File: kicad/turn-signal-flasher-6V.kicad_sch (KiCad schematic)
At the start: 21 parts, among them J1 Conn_Blade, J2 Conn_Blade, J3 Conn_Blade, Q1 BC327, Q2 YJD70P03A, U1 ATtiny45-20P, U2 LM337_TO92

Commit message: add init FW
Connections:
- net at R8.1, R9.2: now also U1.3 (XTAL2/PB4); no longer U1.7 (PB2)
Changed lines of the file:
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@@
+	(wire
+		(pts
+			(xy 115.57 64.77) (xy 115.57 100.33)
+		)
+		(stroke
+			(width 0)
+			(type default)
+		)
+	)
+	(wire
+		(pts
+			(xy 139.7 67.31) (xy 139.7 100.33)
+		)
+		(stroke
+			(width 0)
+			(type default)
+		)
+	)
 	(wire
 		(pts
@@
 	(wire
 		(pts
-			(xy 139.7 62.23) (xy 106.68 62.23)
-		)
-		(stroke
-			(width 0)
-			(type default)
-		)
-	)
-	(wire
-		(pts
 			(xy 195.58 68.58) (xy 214.63 68.58)
 		)
@@
 	(wire
 		(pts
-			(xy 115.57 64.77) (xy 106.68 64.77)
+			(xy 106.68 67.31) (xy 139.7 67.31)
 		)
 		(stroke
@@
 	(wire
 		(pts
-			(xy 115.57 100.33) (xy 115.57 64.77)
-		)
-		(stroke
-			(width 0)
-			(type default)
-		)
-	)
-	(wire
-		(pts
 			(xy 195.58 34.29) (xy 195.58 36.83)
 		)
@@
 	(wire
 		(pts
+			(xy 106.68 64.77) (xy 115.57 64.77)
+		)
+		(stroke
+			(width 0)
+			(type default)
+		)
+	)
+	(wire
+		(pts
 			(xy 173.99 110.49) (xy 173.99 113.03)
 		)
@@
 		)
 		(stroke
-			(width 0)
-			(type default)
-		)
-	)
-	(wire
-		(pts
-			(xy 139.7 62.23) (xy 139.7 100.33)
-		)
-		(stroke

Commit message: finalize PCB and code
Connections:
- no-connect marks 0 -> 3
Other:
- title: (none) -> Turn signal flasher 6 V

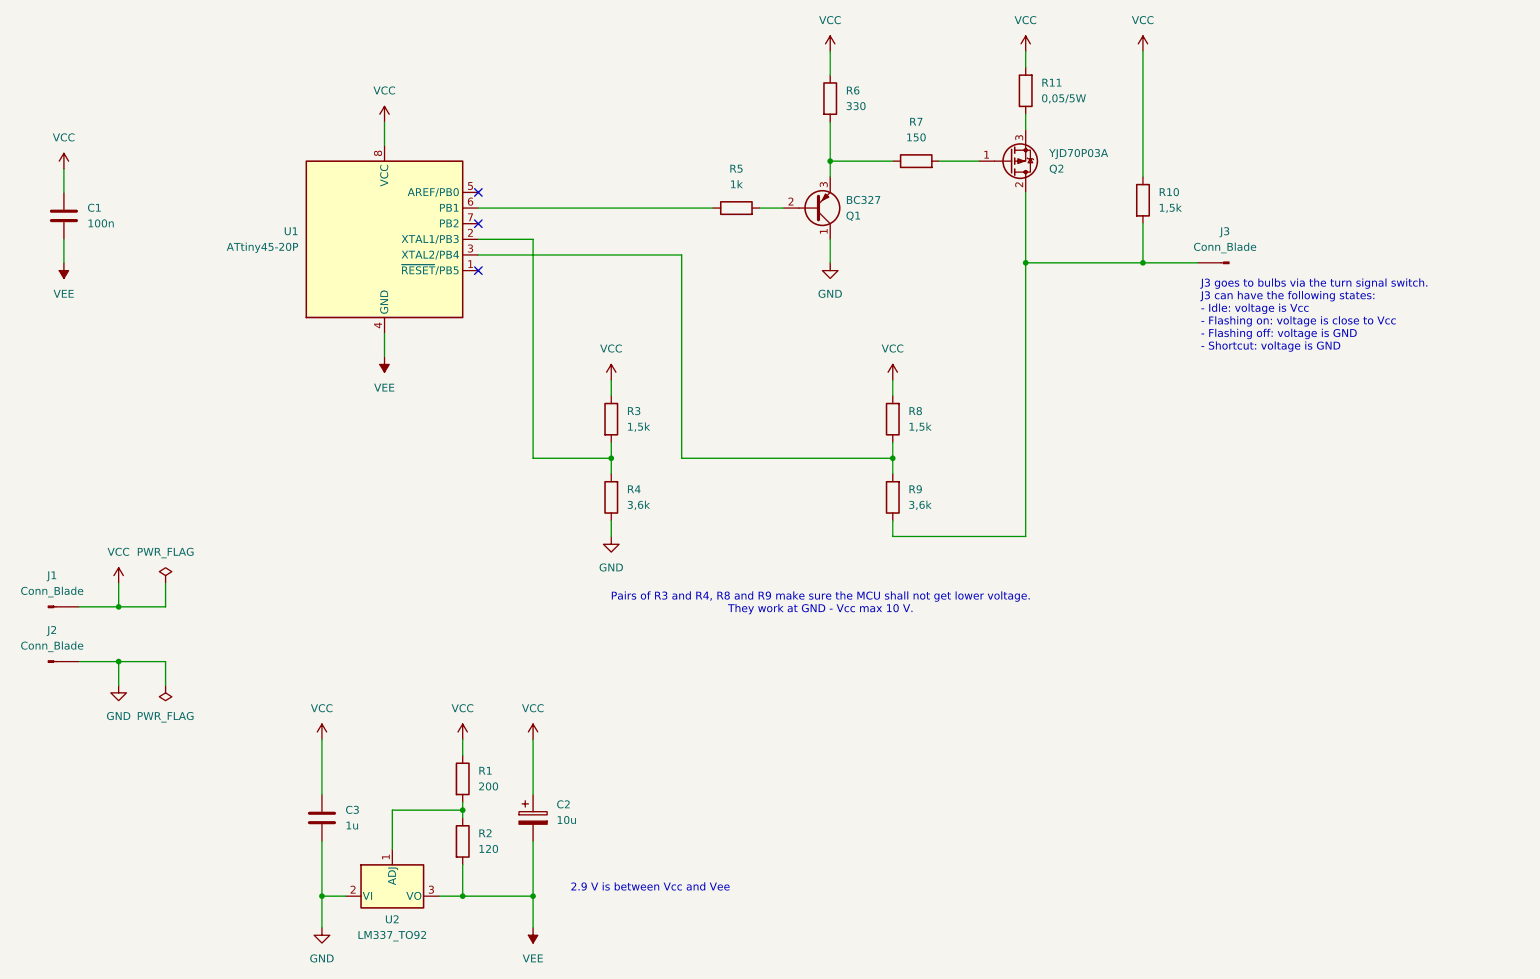
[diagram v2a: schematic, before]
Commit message: fix: overshoot of MOSFET
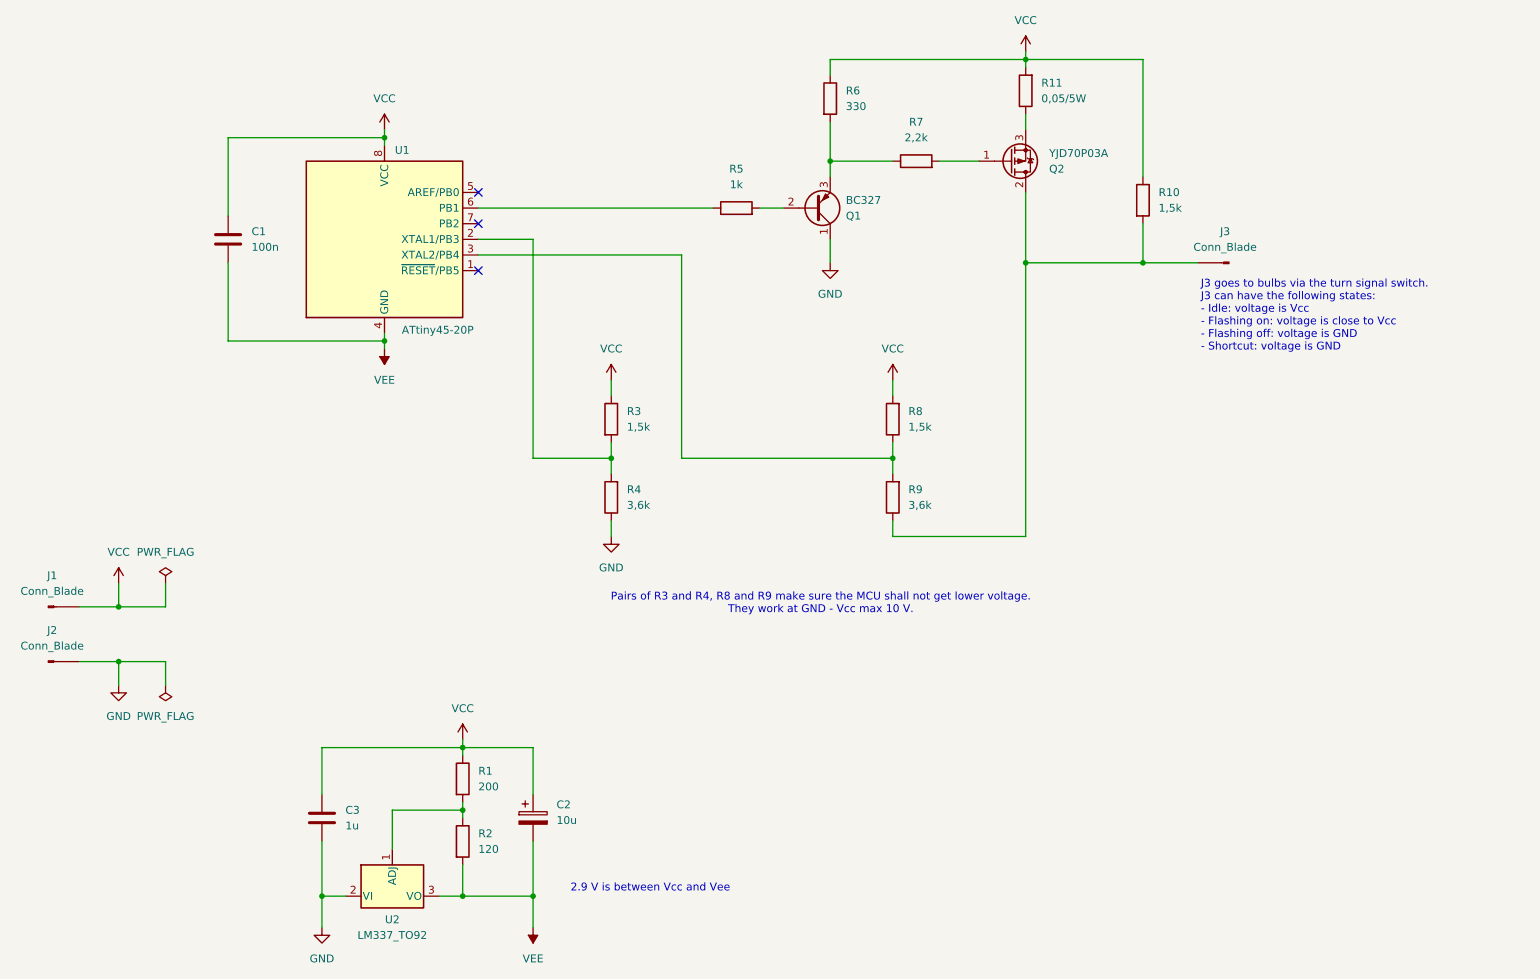
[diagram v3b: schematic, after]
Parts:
- R7: value 150 -> 2,2k
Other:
- moved on the sheet: C1
